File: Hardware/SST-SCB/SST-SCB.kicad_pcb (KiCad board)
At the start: 2 copper layers, 62 x 24 mm, 13 parts, among them J1 MJ-179PH, J2 Conn_01x03_Pin, J3 Conn_01x04_Pin, Q1 2SJ498-D, U1 FT231XS_Breakout, U2 LT1785AxN8

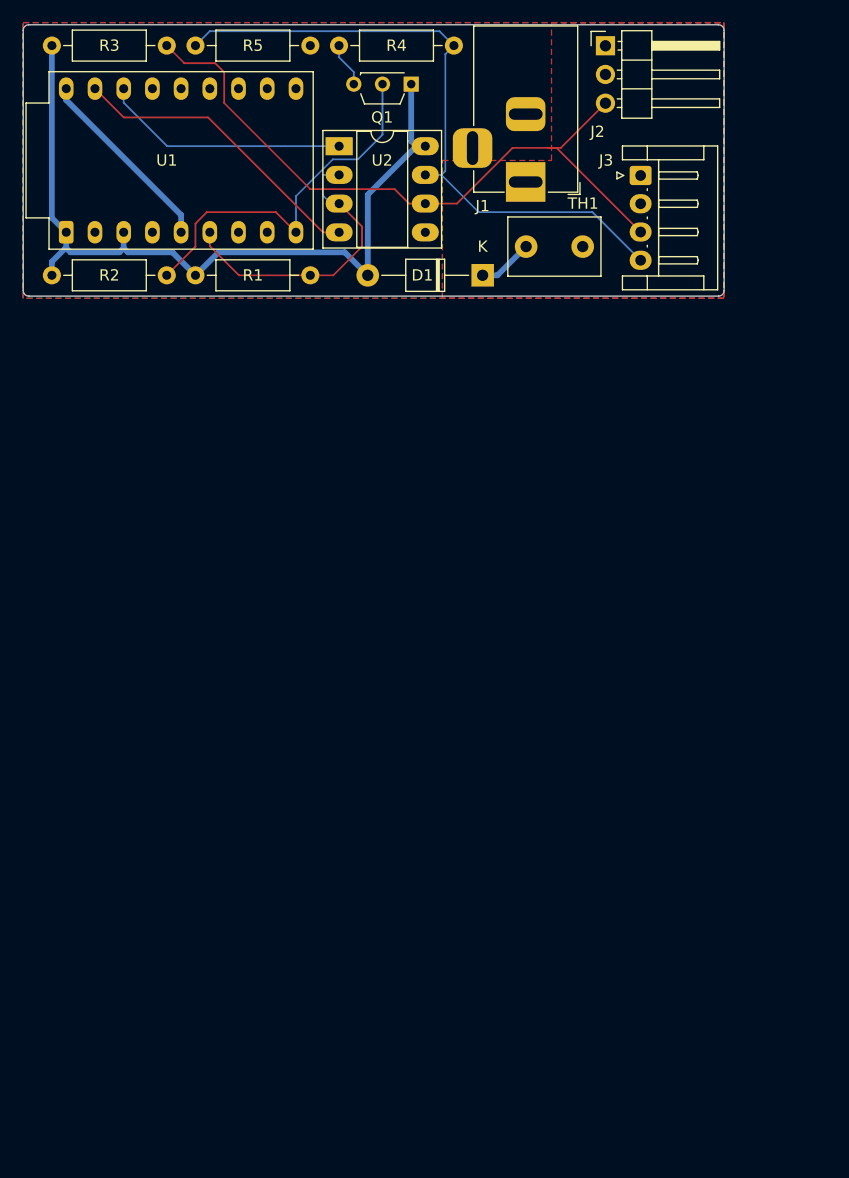
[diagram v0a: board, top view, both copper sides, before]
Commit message: Commit Serial Servo Tester for Servo Control Board
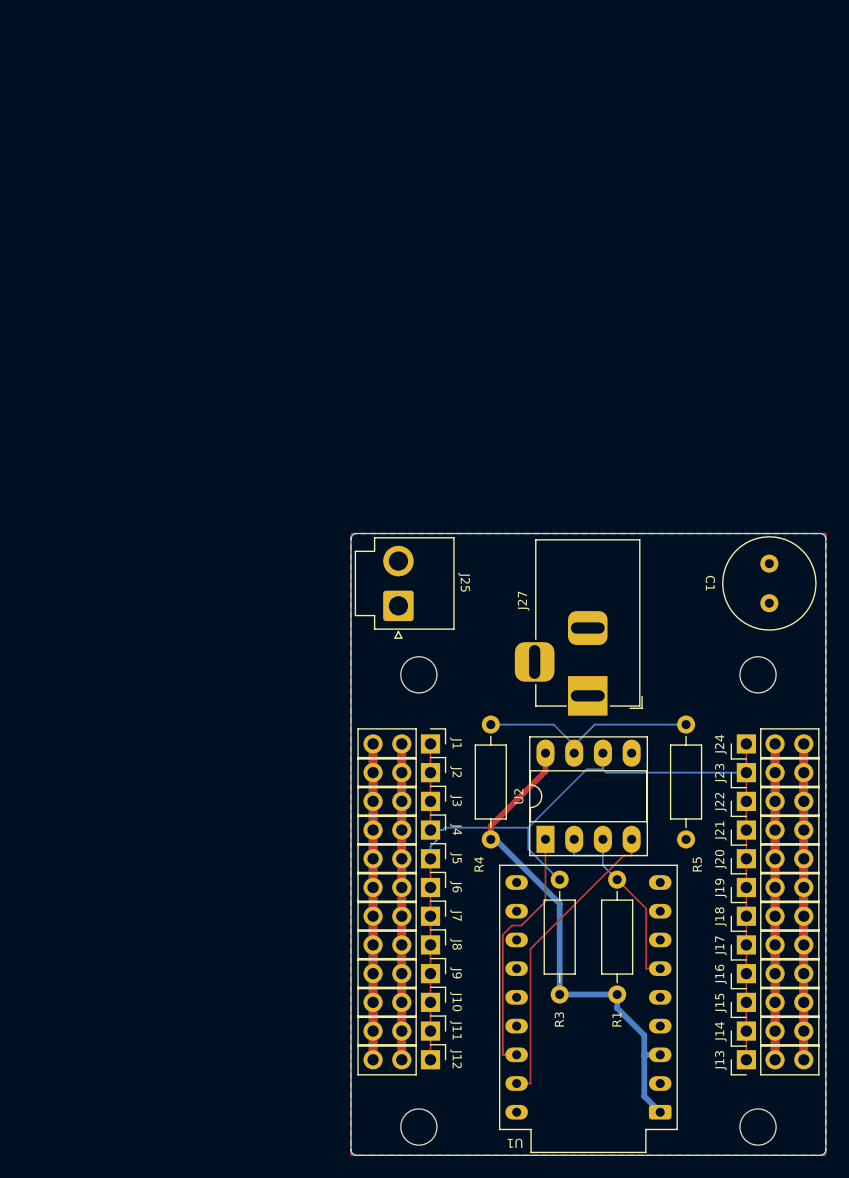
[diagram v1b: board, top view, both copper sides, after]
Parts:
- removed D1: 11EQS03L, Diode_THT:D_T-1_P10.16mm_Horizontal
- removed Q1: 2SJ498-D, Package_TO_SOT_THT:TO-92S_Wide
- removed R2: 5.1k, Resistor_THT:R_Axial_DIN0207_L6.3mm_D2.5mm_P10.16mm_Horizontal
- removed TH1: PTGL07AR820M9A51B0, Capacitor_THT:C_Disc_D8.0mm_W5.0mm_P5.00mm
- added C1: C, Capacitor_THT:C_Radial_D8.0mm_H11.5mm_P3.50mm, F.Cu at (166.0, 101.2)
- added H1: MountingHole, MountingHole:MountingHole_3.2mm_M3, F.Cu at (135.0, 107.5)
- added H2: MountingHole, MountingHole:MountingHole_3.2mm_M3, F.Cu at (135.0, 147.5)
- added H3: MountingHole, MountingHole:MountingHole_3.2mm_M3, F.Cu at (165.0, 147.5)
- added H4: MountingHole, MountingHole:MountingHole_3.2mm_M3, F.Cu at (165.0, 107.5)
- added J10: Conn_01x03_Pin, Connector_PinHeader_2.54mm:PinHeader_1x03_P2.54mm_Vertical, F.Cu at (136.0, 136.5)
- added J11: Conn_01x03_Pin, Connector_PinHeader_2.54mm:PinHeader_1x03_P2.54mm_Vertical, F.Cu at (136.0, 139.0)
- added J12: Conn_01x03_Pin, Connector_PinHeader_2.54mm:PinHeader_1x03_P2.54mm_Vertical, F.Cu at (136.0, 141.6)
- added J13: Conn_01x03_Pin, Connector_PinHeader_2.54mm:PinHeader_1x03_P2.54mm_Vertical, F.Cu at (164.0, 141.6)
- added J14: Conn_01x03_Pin, Connector_PinHeader_2.54mm:PinHeader_1x03_P2.54mm_Vertical, F.Cu at (164.0, 139.0)
- added J15: Conn_01x03_Pin, Connector_PinHeader_2.54mm:PinHeader_1x03_P2.54mm_Vertical, F.Cu at (164.0, 136.5)
- added J16: Conn_01x03_Pin, Connector_PinHeader_2.54mm:PinHeader_1x03_P2.54mm_Vertical, F.Cu at (164.0, 133.9)
- added J17: Conn_01x03_Pin, Connector_PinHeader_2.54mm:PinHeader_1x03_P2.54mm_Vertical, F.Cu at (164.0, 131.4)
- added J18: Conn_01x03_Pin, Connector_PinHeader_2.54mm:PinHeader_1x03_P2.54mm_Vertical, F.Cu at (164.0, 128.8)
- added J19: Conn_01x03_Pin, Connector_PinHeader_2.54mm:PinHeader_1x03_P2.54mm_Vertical, F.Cu at (164.0, 126.3)
- added J20: Conn_01x03_Pin, Connector_PinHeader_2.54mm:PinHeader_1x03_P2.54mm_Vertical, F.Cu at (164.0, 123.8)
- added J21: Conn_01x03_Pin, Connector_PinHeader_2.54mm:PinHeader_1x03_P2.54mm_Vertical, F.Cu at (164.0, 121.2)
- added J22: Conn_01x03_Pin, Connector_PinHeader_2.54mm:PinHeader_1x03_P2.54mm_Vertical, F.Cu at (164.0, 118.7)
- added J23: Conn_01x03_Pin, Connector_PinHeader_2.54mm:PinHeader_1x03_P2.54mm_Vertical, F.Cu at (164.0, 116.2)
- added J24: Conn_01x03_Pin, Connector_PinHeader_2.54mm:PinHeader_1x03_P2.54mm_Vertical, F.Cu at (164.0, 113.6)
- added J25: Conn_01x02_Pin, Connector_JST:JST_VH_B2P-VH_1x02_P3.96mm_Vertical, F.Cu at (133.2, 101.4)
- added J27: MJ-179PH, Connector_BarrelJack:BarrelJack_Horizontal, F.Cu at (149.9, 109.4)
- added J4: Conn_01x03_Pin, Connector_PinHeader_2.54mm:PinHeader_1x03_P2.54mm_Vertical, F.Cu at (136.0, 121.2)
- added J5: Conn_01x03_Pin, Connector_PinHeader_2.54mm:PinHeader_1x03_P2.54mm_Vertical, F.Cu at (136.0, 123.8)
- added J6: Conn_01x03_Pin, Connector_PinHeader_2.54mm:PinHeader_1x03_P2.54mm_Vertical, F.Cu at (136.0, 126.3)
- added J7: Conn_01x03_Pin, Connector_PinHeader_2.54mm:PinHeader_1x03_P2.54mm_Vertical, F.Cu at (136.0, 128.8)
- added J8: Conn_01x03_Pin, Connector_PinHeader_2.54mm:PinHeader_1x03_P2.54mm_Vertical, F.Cu at (136.0, 131.4)
- added J9: Conn_01x03_Pin, Connector_PinHeader_2.54mm:PinHeader_1x03_P2.54mm_Vertical, F.Cu at (136.0, 133.9)
- J1: value MJ-179PH -> Conn_01x03_Pin; footprint Connector_BarrelJack:BarrelJack_Horizontal -> Connector_PinHeader_2.54mm:PinHeader_1x03_P2.54mm_Vertical
- J2: footprint Connector_PinHeader_2.54mm:PinHeader_1x03_P2.54mm_Horizontal -> Connector_PinHeader_2.54mm:PinHeader_1x03_P2.54mm_Vertical
- J3: value Conn_01x04_Pin -> Conn_01x03_Pin; footprint Connector_JST:JST_EH_S4B-EH_1x04_P2.50mm_Horizontal -> Connector_PinHeader_2.54mm:PinHeader_1x03_P2.54mm_Vertical
- moved U1 82.3 mm to (150.0, 136.0), turned to 90 degrees
- moved R3 81.6 mm to (147.5, 125.6), turned to -90 degrees
- moved R5 77.7 mm to (158.6, 122.1), turned to 90 degrees
- moved J2 66.1 mm to (136.0, 116.2), turned to -90 degrees
- moved U2 64.0 mm to (146.2, 122.0), turned to 90 degrees
- moved R4 60.1 mm to (141.4, 111.9), turned to -90 degrees
- moved R1 60.0 mm to (152.5, 125.6), turned to -90 degrees
- moved J3 58.4 mm to (136.0, 118.7)
- moved J1 50.4 mm to (136.0, 113.6)
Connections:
- J1 pad 1: VCC -> /RS485A
- J1 pad 2: GND -> VCC
- J2 pad 1: GND -> /RS485A
- J2 pad 3: /RS485A -> GND
- J3 pad 1: GND -> /RS485A
- J3 pad 3: /RS485A -> GND
- R1 pad 2: Net-(D1-A) -> Net-(U1-5V)
- R3 pad 2: Net-(D1-A) -> Net-(U1-5V)
- R4 pad 2: Net-(Q1-S) -> Net-(U1-5V)
- U1 pad 1: Net-(D1-A) -> Net-(U1-5V)
- U1 pad 3: Net-(D1-A) -> Net-(U1-5V)
- U1 pad 9: /~{EN_4PIN} -> unconnected-(U1-CBUS3-Pad9)
- U2 pad 8: Net-(D1-A) -> Net-(U1-5V)
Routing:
- net VCC: track 0.00 -> 111.8 mm
- net GND: track 16.9 -> 111.8 mm
- net Net-(D1-A): track 72.2 -> 0.00 mm
- net Net-(U1-5V): track 0.00 -> 44.6 mm
- net /RS485B: track 58.0 -> 19.5 mm
- net /~{EN_4PIN}: track 33.2 -> 0.00 mm
- net /RS485A: track 61.1 -> 93.6 mm
- net Net-(U1-CBUS0): track 26.4 -> 18.2 mm
- net Net-(D1-K): track 4.90 -> 0.00 mm
- net Net-(Q1-S): track 3.95 -> 0.00 mm
- removed copper zone on F.Cu, net GND
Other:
- board size 62 x 24 mm -> 42 x 55 mm
- board text added: "SST-SCB github.com/rmf-hru-wg/SerialServoTester"
